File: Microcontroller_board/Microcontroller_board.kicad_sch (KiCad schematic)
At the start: 1 part, among them U1 ESP32-WROOM-E

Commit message: Upload of microcontroller schematic updates
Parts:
- added C1, C4: 0.1 uF, symbol Device:C_Small
- added C2: 22 uF, symbol Device:C_Polarized_Small
- added C3: 1 uF, symbol Device:C_Polarized_Small
- added D1: Power_Led, symbol Device:LED
- added R1, R2: 10 k, symbol Device:R_Small
- added R3: 330 R, symbol Device:R_Small
- added SW1: SW_Reset, symbol Switch:SW_Push
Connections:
- net GND: now also C1.2, C2.2, C3.2, C4.2, D1.1 (K), SW1.2
- net +3.3V: now reaches U1.2 (3V3)
- net +3.3V: now also C1.1, C2.1, R1.1, R3.1
- net EN: now reaches U1.3 (EN/CHIP_PU)
- net EN: now also C3.1, R1.2, R2.1
- new net: C4.1, R2.2, SW1.1
- new net: D1.2 (A), R3.2

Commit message: Add cp2102 schematic
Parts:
- added C5, C7: 0.1 uF, symbol Device:C_Small
- added C6: 1 uF, symbol Device:C_Polarized_Small
- added C8: 4.7 uF, symbol Device:C_Polarized_Small
- added D2: SP0503BAHT, Package_TO_SOT_SMD:SOT-143, symbol Power_Protection:SP0503BAHT
- added J1: USB_B_Micro, symbol Connector:USB_B_Micro
- added Q1, Q2: BC817, Package_TO_SOT_SMD:SOT-23, symbol Transistor_BJT:BC817
- added R4, R5, R6, R7: 10k, symbol Device:R_Small
- added U2: CP2102N-Axx-xQFN28, Package_DFN_QFN:QFN-28-1EP_5x5mm_P0.5mm_EP3.35x3.35mm, symbol Interface_USB:CP2102N-Axx-xQFN28
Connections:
- net EN: now also Q1.3 (C)
- net GND: now also C5.2, C6.2, C7.2, C8.2, D2.1 (A), J1.5 (GND), J1.6 (Shield), R4.2, U2.29 (GND), U2.3 (GND)
- net IO0: now reaches U1.25 (GPIO0/BOOT/ADC2_CH1)
- net IO0: now also Q2.2 (E)
- net RX0: now reaches U1.34 (U0RXD/GPIO3)
- net RX0: now also U2.26 (TXD)
- net TX0: now reaches U1.35 (U0TXD/GPIO1)
- net TX0: now also U2.25 (RXD)
- new net: Q2.1 (B), R7.2
- new net: Q1.1 (B), R6.2
- new net: R4.1, U2.11 (~{SUSPEND})
- new net: R5.2, U2.9 (~{RST})
- new net DTR: Q2.3 (C), R6.1, U2.28 (~{DTR})
- new net RTS: Q1.2 (E), R7.1, U2.24 (~{RTS})
- new net USB_D+: D2.3 (K), J1.3 (D+), U2.4 (D+)
- new net USB_D-: D2.4 (K), J1.2 (D-), U2.5 (D-)
- new net VBUS: C5.1, C6.1, D2.2 (K), J1.1 (VBUS), U2.7 (VREGIN), U2.8 (VBUS)
- new net VDD: C7.1, C8.1, R5.1, U2.6 (VDD)
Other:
- note added: "CP2102"
- note added: "ESP32"
- moved on the sheet: C1, C2, C3, C4, D1, R1, R2, R3, SW1, U1

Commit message: CP2102 circuit updated
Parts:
- added C9: 0.1 uF, symbol Device:C_Small
- added J2: Conn_01x07_Pin, symbol Connector:Conn_01x07_Pin
- R6, R7: value 10k -> 12k
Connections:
- net +3.3V: now also C7.1, C8.1, R5.1, J2.7 (Pin_7)
- net DTR: now also J2.2 (Pin_2)
- net GND: now also C9.1, J2.6 (Pin_6)
- net RTS: now also J2.1 (Pin_1)
- net RX0: now also J2.4 (Pin_4)
- net TX0: now also J2.3 (Pin_3)
- removed net VDD: C7.1, C8.1, R5.1, U2.6 (VDD)
- new net: C9.2, U2.6 (VDD)
- new net +5V: J2.5 (Pin_5)
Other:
- note added: "Auto programming circuit"
- note added: "Aux. programming circuit"
- moved on the sheet: C5, C6, C7, C8, D2, J1, Q1, Q2, R5, R6, R7

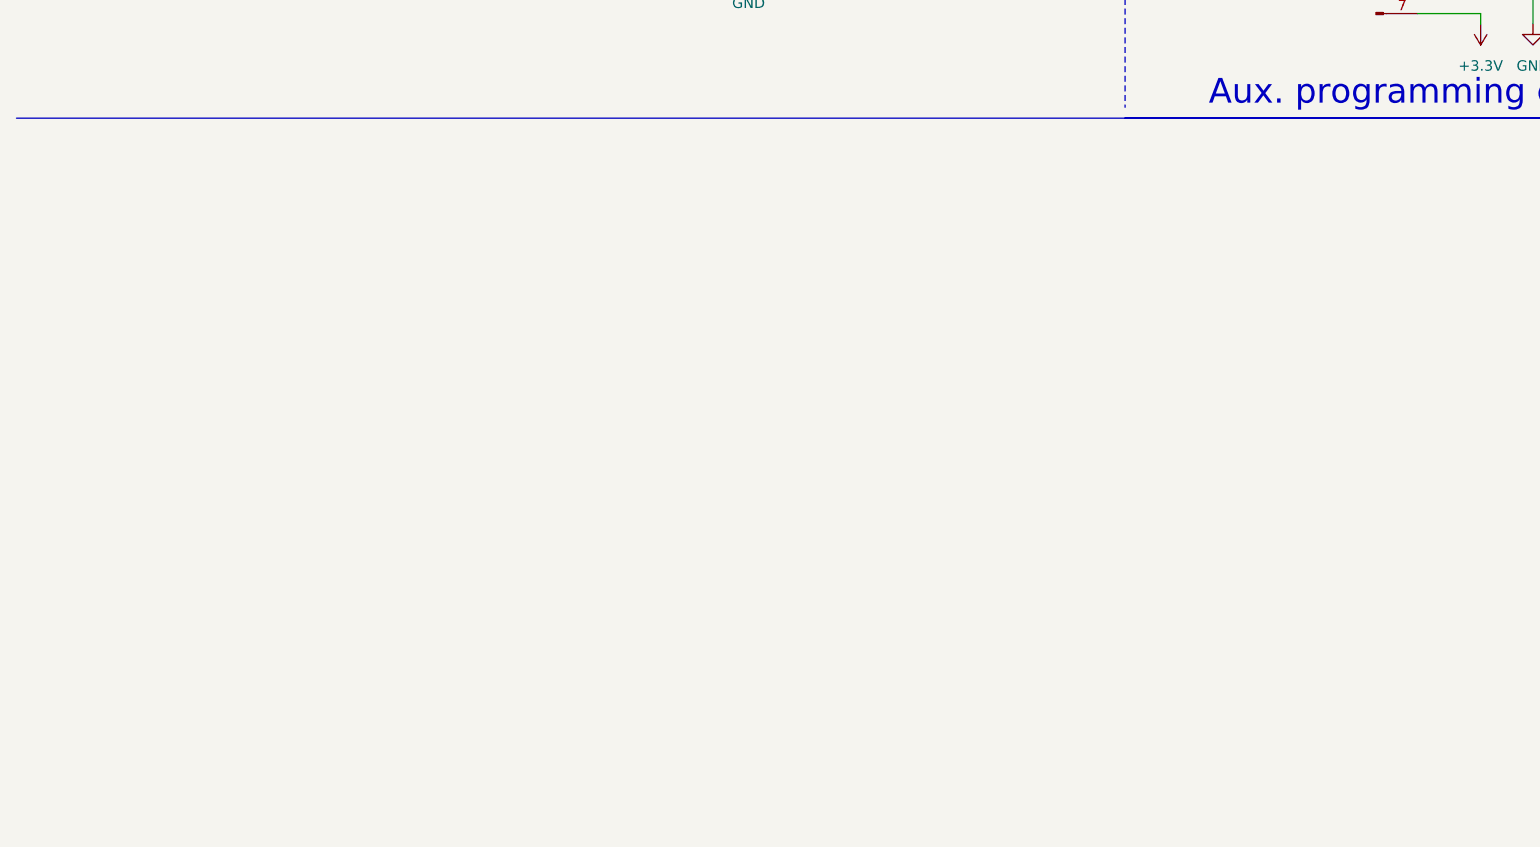
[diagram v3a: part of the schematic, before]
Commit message: Agregado del circuito de traba para el conector
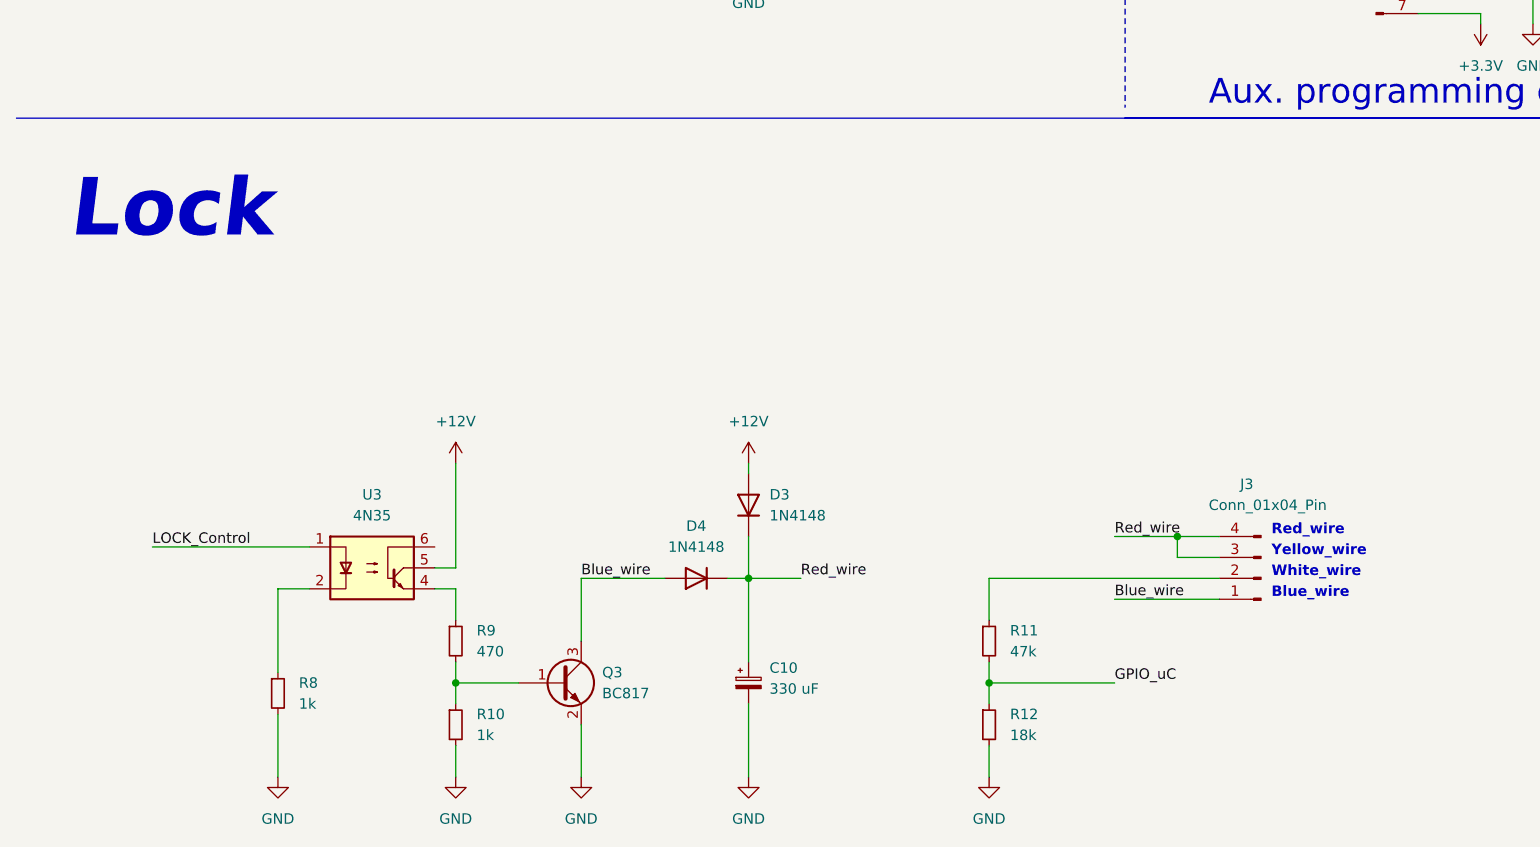
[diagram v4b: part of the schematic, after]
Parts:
- added C10: 330 uF, symbol Device:C_Polarized_Small
- added D3, D4: 1N4148, Diode_THT:D_DO-35_SOD27_P7.62mm_Horizontal, symbol Diode:1N4148
- added J3: Conn_01x04_Pin, symbol Connector:Conn_01x04_Pin
- added Q3: BC817, Package_TO_SOT_SMD:SOT-23, symbol Transistor_BJT:BC817
- added R10, R8: 1k, symbol Device:R_Small
- added R11: 47k, symbol Device:R_Small
- added R12: 18k, symbol Device:R_Small
- added R9: 470, symbol Device:R_Small
- added U3: 4N35, Package_DIP:DIP-6_W7.62mm, symbol Isolator:4N35
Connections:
- net GND: now also C10.2, Q3.2 (E), R10.2, R12.2, R8.2
- new net: J3.2 (Pin_2), R11.1
- new net: R8.1, U3.2
- new net: R9.1, U3.4
- new net: Q3.1 (B), R10.1, R9.2
- new net +12V: D3.2 (A), U3.5
- new net Blue_wire: D4.2 (A), J3.1 (Pin_1), Q3.3 (C)
- new net GPIO_uC: R11.2, R12.1
- new net LOCK_Control: U3.1
- new net Red_wire: C10.1, D3.1 (K), D4.1 (K), J3.3 (Pin_3), J3.4 (Pin_4)
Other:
- note added: "Blue_wire"
- note added: "Lock"
- note added: "Red_wire"
- note added: "White_wire"
- note added: "Yellow_wire"

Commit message: I changed the format of the root project, now it has different pages for peripherals
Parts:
- removed C1, C4, C5, C7, C9: 0.1 uF, symbol Device:C_Small
- removed C10: 330 uF, symbol Device:C_Polarized_Small
- removed C2: 22 uF, symbol Device:C_Polarized_Small
- removed C3, C6: 1 uF, symbol Device:C_Polarized_Small
- removed C8: 4.7 uF, symbol Device:C_Polarized_Small
- removed D1: Power_Led, symbol Device:LED
- removed D2: SP0503BAHT, Package_TO_SOT_SMD:SOT-143, symbol Power_Protection:SP0503BAHT
- removed D3, D4: 1N4148, Diode_THT:D_DO-35_SOD27_P7.62mm_Horizontal, symbol Diode:1N4148
- removed J1: USB_B_Micro, symbol Connector:USB_B_Micro
- removed J2: Conn_01x07_Pin, symbol Connector:Conn_01x07_Pin
- removed J3: Conn_01x04_Pin, symbol Connector:Conn_01x04_Pin
- removed Q1, Q2, Q3: BC817, Package_TO_SOT_SMD:SOT-23, symbol Transistor_BJT:BC817
- removed R1, R2: 10 k, symbol Device:R_Small
- removed R10, R8: 1k, symbol Device:R_Small
- removed R11: 47k, symbol Device:R_Small
- removed R12: 18k, symbol Device:R_Small
- removed R3: 330 R, symbol Device:R_Small
- removed R4, R5: 10k, symbol Device:R_Small
- removed R6, R7: 12k, symbol Device:R_Small
- removed R9: 470, symbol Device:R_Small
- removed SW1: SW_Reset, symbol Switch:SW_Push
- removed U1: ESP32-WROOM-E, PCM_Espressif:ESP32-WROOM-32E, symbol PCM_Espressif:ESP32-WROOM-E
- removed U2: CP2102N-Axx-xQFN28, Package_DFN_QFN:QFN-28-1EP_5x5mm_P0.5mm_EP3.35x3.35mm, symbol Interface_USB:CP2102N-Axx-xQFN28
- removed U3: 4N35, Package_DIP:DIP-6_W7.62mm, symbol Isolator:4N35
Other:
- added sheet CP2102 Programmer (programmer.kicad_sch)
- added sheet Connector lock (ConnectorLock.kicad_sch)
- added sheet Microcontroller (Microcontroller.kicad_sch)
- note removed: "Auto programming circuit"
- note removed: "Aux. programming circuit"
- note removed: "Blue_wire"
- note removed: "CP2102"
- note removed: "ESP32"
- note removed: "Lock"
- note removed: "Red_wire"
- note removed: "White_wire"
- note removed: "Yellow_wire"

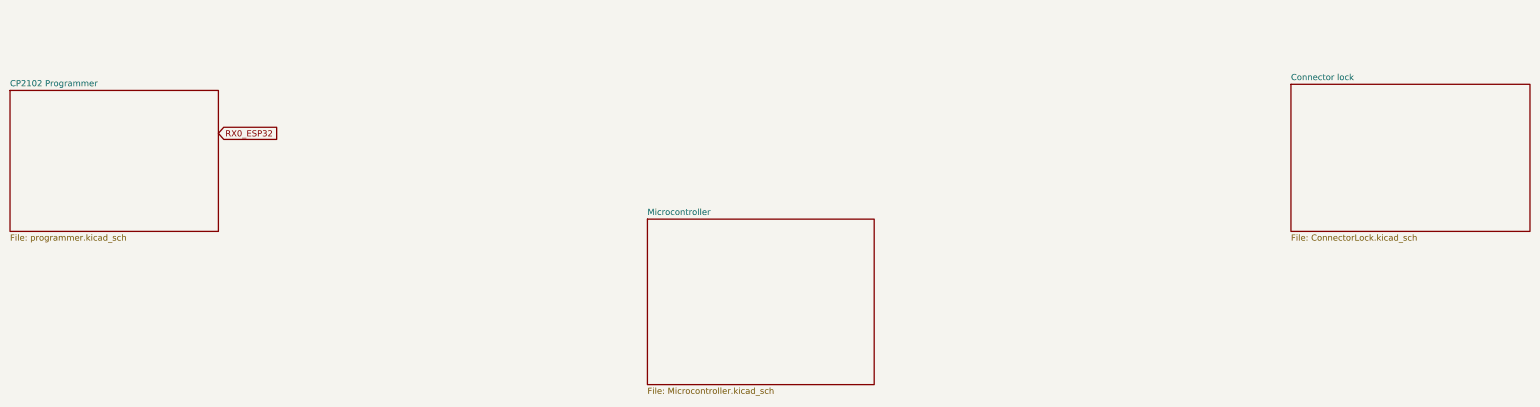
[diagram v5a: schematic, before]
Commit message: Added more pages, CP and RS485
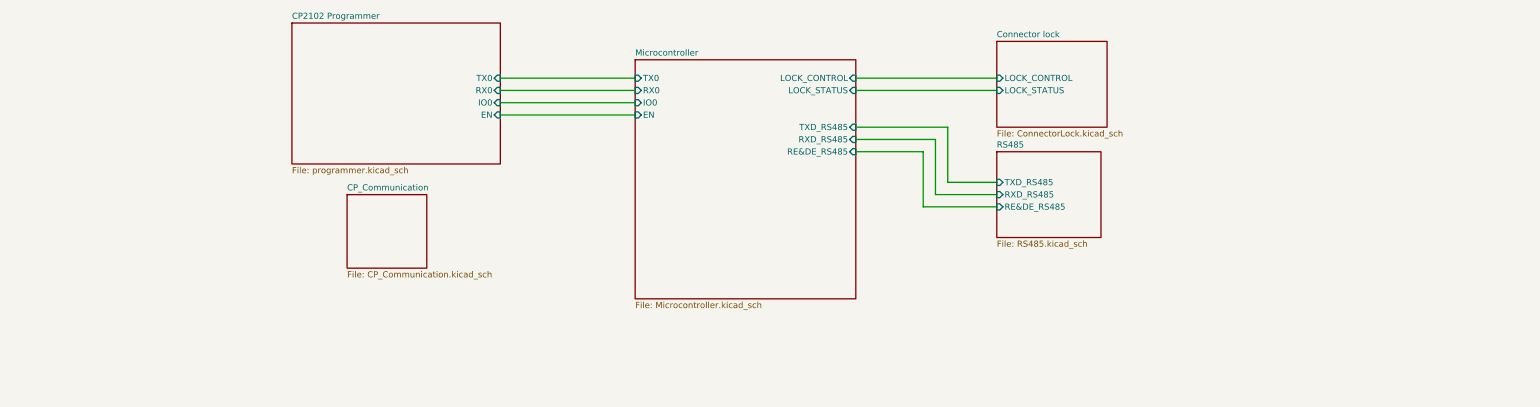
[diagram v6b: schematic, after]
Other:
- added sheet CP_Communication (CP_Communication.kicad_sch)
- added sheet RS485 (RS485.kicad_sch)
- sheet CP2102 Programmer ports: added EN, IO0, RX0, TX0; removed none
- sheet Connector lock ports: added LOCK_CONTROL, LOCK_STATUS; removed none
- sheet Microcontroller ports: added EN, IO0, LOCK_CONTROL, LOCK_STATUS, RE&DE_RS485, RX0, RXD_RS485, TX0, TXD_RS485; removed none
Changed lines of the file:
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@@
 (kicad_sch (version 20230121) (generator eeschema)
   (paper "A3")
-  (global_label "RX0_ESP32" (shape input) (at 92.71 53.34 0) (fields_autoplaced)
-    (effects (font (size 1.27 1.27)) (justify left))
-    (property "Intersheetrefs" "${INTERSHEET_REFS}" (at 106.3993 53.34 0)
-      (effects (font (size 1.27 1.27)) (justify left) hide)
+  (wire (pts (xy 151.13 49.53) (xy 179.07 49.53))
+    (stroke (width 0) (type default))
+  )
+  (wire (pts (xy 224.79 44.45) (xy 254 44.45))
+    (stroke (width 0) (type default))
+  )
+  (wire (pts (xy 243.84 52.07) (xy 243.84 63.5))
+    (stroke (width 0) (type default))
+  )
+  (wire (pts (xy 151.13 44.45) (xy 179.07 44.45))
+    (stroke (width 0) (type default))
+  )
+  (wire (pts (xy 243.84 63.5) (xy 254 63.5))
+    (stroke (width 0) (type default))
+  )
+  (wire (pts (xy 238.76 57.15) (xy 238.76 68.58))
+    (stroke (width 0) (type default))
+  )
+  (wire (pts (xy 254 66.04) (xy 241.3 66.04))
+    (stroke (width 0) (type default))
+  )
+  (wire (pts (xy 238.76 68.58) (xy 254 68.58))
+    (stroke (width 0) (type default))
+  )
+  (wire (pts (xy 151.13 46.99) (xy 179.07 46.99))
+    (stroke (width 0) (type default))
+  )
+  (wire (pts (xy 241.3 54.61) (xy 224.79 54.61))
+    (stroke (width 0) (type default))
+  )
+  (wire (pts (xy 151.13 41.91) (xy 179.07 41.91))
+    (stroke (width 0) (type default))
+  )
+  (wire (pts (xy 224.79 52.07) (xy 243.84 52.07))
+    (stroke (width 0) (type default))
+  )
+  (wire (pts (xy 241.3 66.04) (xy 241.3 54.61))
+    (stroke (width 0) (type default))
+  )
+  (wire (pts (xy 224.79 41.91) (xy 254 41.91))
+    (stroke (width 0) (type default))
+  )
+  (wire (pts (xy 224.79 57.15) (xy 238.76 57.15))
+    (stroke (width 0) (type default))
+  )
+  (sheet (at 254 57.15) (size 21.59 17.78) (fields_autoplaced)
+    (stroke (width 0.1524) (type solid))
+    (fill (color 0 0 0 0.0000))
+    (property "Sheetname" "RS485" (at 254 56.4384 0)
+      (effects (font (size 1.27 1.27)) (justify left bottom))
+    )
+    (property "Sheetfile" "RS485.kicad_sch" (at 254 75.5146 0)
+      (effects (font (size 1.27 1.27)) (justify left top))
+    )
+    (pin "TXD_RS485" input (at 254 63.5 180)
+      (effects (font (size 1.27 1.27)) (justify left))
+    )
+    (pin "RXD_RS485" input (at 254 66.04 180)
+      (effects (font (size 1.27 1.27)) (justify left))
+    )
+    (pin "RE&DE_RS485" input (at 254 68.58 180)
+      (effects (font (size 1.27 1.27)) (justify left))
+    )
+    (instances
+      (project "Microcontroller_board"
+        (path "/8159cf7c-7477-4d57-9227-35cab5afcf8d" (page "5"))
+      )
     )
   )
-  (sheet (at 314.96 43.18) (size 49.53 30.48) (fields_autoplaced)
+  (sheet (at 254 34.29) (size 22.86 17.78) (fields_autoplaced)
     (stroke (width 0.1524) (type solid))
     (fill (color 0 0 0 0.0000))
-    (property "Sheetname" "Connector lock" (at 314.96 42.4684 0)
+    (property "Sheetname" "Connector lock" (at 254 33.5784 0)
       (effects (font (size 1.27 1.27)) (justify left bottom))
     )
-    (property "Sheetfile" "ConnectorLock.kicad_sch" (at 314.96 74.2446 0)
+    (property "Sheetfile" "ConnectorLock.kicad_sch" (at 254 52.6546 0)
       (effects (font (size 1.27 1.27)) (justify left top))
+    )
+    (pin "LOCK_CONTROL" input (at 254 41.91 180)
+      (effects (font (size 1.27 1.27)) (justify left))
+    )
+    (pin "LOCK_STATUS" input (at 254 44.45 180)
+      (effects (font (size 1.27 1.27)) (justify left))
     )
     (instances
@@
     )
   )
-  (sheet (at 49.53 44.45) (size 43.18 29.21) (fields_autoplaced)
+  (sheet (at 107.95 30.48) (size 43.18 29.21) (fields_autoplaced)
     (stroke (width 0.1524) (type solid))
     (fill (color 0 0 0 0.0000))
-    (property "Sheetname" "CP2102 Programmer" (at 49.53 43.7384 0)
+    (property "Sheetname" "CP2102 Programmer" (at 107.95 29.7684 0)
       (effects (font (size 1.27 1.27)) (justify left bottom))
     )
-    (property "Sheetfile" "programmer.kicad_sch" (at 49.53 74.2446 0)
+    (property "Sheetfile" "programmer.kicad_sch" (at 107.95 60.2746 0)
       (effects (font (size 1.27 1.27)) (justify left top))
+    )
+    (pin "TX0" input (at 151.13 41.91 0)
+      (effects (font (size 1.27 1.27)) (justify right))
+    )
+    (pin "RX0" input (at 151.13 44.45 0)
+      (effects (font (size 1.27 1.27)) (justify right))
+    )
+    (pin "IO0" input (at 151.13 46.99 0)
+      (effects (font (size 1.27 1.27)) (justify right))
+    )
+    (pin "EN" input (at 151.13 49.53 0)
+      (effects (font (size 1.27 1.27)) (justify right))
     )
     (instances
@@
     )
   )
-  (sheet (at 181.61 71.12) (size 46.99 34.29) (fields_autoplaced)
+  (sheet (at 119.38 66.04) (size 16.51 15.24) (fields_autoplaced)
     (stroke (width 0.1524) (type solid))
     (fill (color 0 0 0 0.0000))
-    (property "Sheetname" "Microcontroller" (at 181.61 70.4084 0)
+    (property "Sheetname" "CP_Communication" (at 119.38 65.3284 0)
       (effects (font (size 1.27 1.27)) (justify left bottom))
     )
-    (property "Sheetfile" "Microcontroller.kicad_sch" (at 181.61 105.9946 0)
+    (property "Sheetfile" "CP_Communication.kicad_sch" (at 119.38 81.8646 0)
       (effects (font (size 1.27 1.27)) (justify left top))
     )
     (instances
+      (project "Microcontroller_board"
+        (path "/8159cf7c-7477-4d57-9227-35cab5afcf8d" (page "6"))
+      )
+    )
+  )
+  (sheet (at 179.07 38.1) (size 45.72 49.53) (fields_autoplaced)
+    (stroke (width 0.1524) (type solid))
+    (fill (color 0 0 0 0.0000))
+    (property "Sheetname" "Microcontroller" (at 179.07 37.3884 0)
+      (effects (font (size 1.27 1.27)) (justify left bottom))
+    )
+    (property "Sheetfile" "Microcontroller.kicad_sch" (at 179.07 88.2146 0)
+      (effects (font (size 1.27 1.27)) (justify left top))
+    )
+    (pin "EN" input (at 179.07 49.53 180)
+      (effects (font (size 1.27 1.27)) (justify left))
+    )
+    (pin "RX0" input (at 179.07 44.45 180)
+      (effects (font (size 1.27 1.27)) (justify left))
+    )
+    (pin "IO0" input (at 179.07 46.99 180)
+      (effects (font (size 1.27 1.27)) (justify left))
+    )
+    (pin "TX0" input (at 179.07 41.91 180)
+      (effects (font (size 1.27 1.27)) (justify left))
+    )
+    (pin "LOCK_STATUS" input (at 224.79 44.45 0)
+      (effects (font (size 1.27 1.27)) (justify right))
+    )
+    (pin "LOCK_CONTROL" input (at 224.79 41.91 0)
+      (effects (font (size 1.27 1.27)) (justify right))
+    )
+    (pin "RXD_RS485" input (at 224.79 54.61 0)
+      (effects (font (size 1.27 1.27)) (justify right))
+    )
+    (pin "RE&DE_RS485" input (at 224.79 57.15 0)
+      (effects (font (size 1.27 1.27)) (justify right))
+    )
+    (pin "TXD_RS485" input (at 224.79 52.07 0)
+      (effects (font (size 1.27 1.27)) (justify right))
+    )
+    (instances
